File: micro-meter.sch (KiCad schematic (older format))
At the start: 143 parts, among them J1 DC_IN, J10 5V_OUT, J2 SPI, J3 I2C / UART, J4 IN1, J5 IN2, J6 IN3, J7 IN4, J8 SWD, J9 USB_B_Micro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

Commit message: Layout blocks
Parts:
- added J11: LEDS_DATA, Connector_PinHeader_2.54mm:PinHeader_1x03_P2.54mm_Vertical, symbol Connector:Conn_01x03_Male
- added J12: LEDS_EXT, Connector_PinHeader_2.54mm:PinHeader_1x03_P2.54mm_Vertical, symbol Connector:Conn_01x03_Male
- added TP10: TP_4V3, TestPoint:TestPoint_Pad_2.0x2.0mm, symbol Connector:TestPoint
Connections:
- net CE is gone; now on net CE+I2S2_MCK: J2.3 (Pin_3)
- net +5V: now also J11.1 (Pin_1), J12.1 (Pin_1)
- net GND: now also J11.3 (Pin_3), J12.3 (Pin_3)
- net I2S5_SD: now also J11.2 (Pin_2)
- net at D30.1 (K), D4.1 (K), D5.1 (K)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: now also TP10.1
- net LEDS_EXT: now reaches D29.2 (DOUT)
- net LEDS_EXT: now also J12.2 (Pin_2)
- no-connect marks 19 -> 18
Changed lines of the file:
@@
 U 1 1 5FA0621D
 P 4600 7200
-F 0 "C16" H 4800 7250 50  0000 R CNN
-F 1 "10u" H 4850 7150 50  0000 R CNN
+F 0 "C16" H 4850 7200 50  0000 R CNN
+F 1 "10u" H 4850 7100 50  0000 R CNN
 F 2 "Capacitor_SMD:C_0603_1608Metric" H 4600 7200 50  0001 C CNN
 F 3 "~" H 4600 7200 50  0001 C CNN
@@
 U 1 1 5FDE2D61
 P 4300 6950
-F 0 "FB3" V 4500 6900 50  0000 L CNN
+F 0 "FB3" V 4200 6800 50  0000 L CNN
 F 1 "600@100MHz" V 4400 6700 50  0000 L CNN
 F 2 "Inductor_SMD:L_0805_2012Metric" V 4230 6950 50  0001 C CNN
@@
 Wire Wire Line
 	10400 5600 10400 5550
-NoConn ~ 10700 5950
 Wire Wire Line
 	4000 6950 4200 6950
@@
 U 1 1 60044435
 P 4000 7150
-F 0 "R14" H 3900 7100 50  0000 R CNN
-F 1 "3k9" H 3900 7200 50  0000 R CNN
+F 0 "R14" H 3900 7150 50  0000 R CNN
+F 1 "3k9" H 3900 7250 50  0000 R CNN
 F 2 "Resistor_SMD:R_0603_1608Metric" V 3930 7150 50  0001 C CNN
 F 3 "~" H 4000 7150 50  0001 C CNN
@@
 Wire Notes Line
 	8800 1900 11200 1900
-Wire Notes Line
-	4750 4000 4750 500
 Wire Notes Line
 	2900 4000 2900 6550
@@
 	0    1    1    0
 $EndComp
-Text GLabel 1200 5000 0    50   Input ~ 0
-CE
 Text GLabel 1200 5100 0    50   Input ~ 0
 SPI2_SCK
@@
 Text Notes 550  6350 0    50   ~ 0
 Input voltage range: 5-24V DC
+$Comp
+L Connector:TestPoint TP10
+U 1 1 5FB52136
+P 4000 6700
+F 0 "TP10" V 4050 6950 50  0000 C CNN
+F 1 "TP_4V3" V 3950 7000 50  0000 C CNN
+F 2 "TestPoint:TestPoint_Pad_2.0x2.0mm" H 4000 6700 50  0001 C CNN
+F 3 "~" H 4000 6700 50  0001 C CNN
+	1    4000 6700
+	0    1    -1   0
+$EndComp
+Connection ~ 4000 6700
+$Comp
+L Connector:Conn_01x03_Male J11
+U 1 1 5FB8F99C
+P 4600 3150
+F 0 "J11" H 4650 3400 50  0000 C CNN
+F 1 "LEDS_DATA" V 4550 3150 50  0000 C CNN
+F 2 "Connector_PinHeader_2.54mm:PinHeader_1x03_P2.54mm_Vertical" H 4600 3150 50  0001 C CNN
+F 3 "~" H 4600 3150 50  0001 C CNN
+	1    4600 3150
+	-1   0    0    -1
+$EndComp
+Text GLabel 4400 3700 0    50   Input ~ 0
+LEDS_EXT
+$Comp
+L power:+5V #PWR0131
+U 1 1 5FB91854
+P 4400 3050
+F 0 "#PWR0131" H 4400 2900 50  0001 C CNN
+F 1 "+5V" H 4550 3100 50  0000 C CNN
+F 2 "" H 4400 3050 50  0001 C CNN
+F 3 "" H 4400 3050 50  0001 C CNN
+	1    4400 3050
+	-1   0    0    -1
+$EndComp
+$Comp
+L power:GND #PWR0132
+U 1 1 5FB92B2A
+P 4400 3250
+F 0 "#PWR0132" H 4400 3000 50  0001 C CNN
+F 1 "GND" H 4550 3200 50  0000 C CNN
+F 2 "" H 4400 3250 50  0001 C CNN
+F 3 "" H 4400 3250 50  0001 C CNN
+	1    4400 3250
+	-1   0    0    -1
+$EndComp
+Text GLabel 1200 5000 0    50   Input ~ 0
+CE+I2S2_MCK
+$Comp
+L Connector:Conn_01x03_Male J12
+U 1 1 5FD53931
+P 4600 3700
+F 0 "J12" H 4650 3950 50  0000 C CNN
+F 1 "LEDS_EXT" V 4550 3700 50  0000 C CNN
+F 2 "Connector_PinHeader_2.54mm:PinHeader_1x03_P2.54mm_Vertical" H 4600 3700 50  0001 C CNN
+F 3 "~" H 4600 3700 50  0001 C CNN
+	1    4600 3700
+	-1   0    0    -1
+$EndComp
+Text GLabel 4400 3150 0    50   Input ~ 0
+I2S5_SD
+$Comp
+L power:+5V #PWR0133
+U 1 1 5FD5393C
+P 4400 3600
+F 0 "#PWR0133" H 4400 3450 50  0001 C CNN
+F 1 "+5V" H 4550 3650 50  0000 C CNN
+F 2 "" H 4400 3600 50  0001 C CNN
+F 3 "" H 4400 3600 50  0001 C CNN
+	1    4400 3600
+	-1   0    0    -1
+$EndComp
+$Comp
+L power:GND #PWR0134
+U 1 1 5FD53946
+P 4400 3800
+F 0 "#PWR0134" H 4400 3550 50  0001 C CNN
+F 1 "GND" H 4550 3750 50  0000 C CNN
+F 2 "" H 4400 3800 50  0001 C CNN
+F 3 "" H 4400 3800 50  0001 C CNN
+	1    4400 3800
+	-1   0    0    -1
+$EndComp
+Wire Notes Line
+	4750 50   4750 4000
+Text GLabel 10900 6000 3    50   Output ~ 0
+LEDS_EXT
+Wire Wire Line
+	10900 6000 10900 5950
+Wire Wire Line
+	10900 5950 10700 5950
 $EndSCHEMATC

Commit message: Rough layout
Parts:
- removed TP3: TP_5V, TestPoint:TestPoint_Pad_2.0x2.0mm, symbol Connector:TestPoint
- removed U5: USBLC6-2SC6, Package_TO_SOT_SMD:SOT-23-6, symbol Power_Protection:USBLC6-2SC6
- L1: footprint Inductor_SMD:L_Sunlord_MWSA0518_5.4x5.2mm -> Inductor_SMD:L_TDK_NLV25_2.5x2.0mm
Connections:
- net USB_CON_D+ is gone; now on net USB_D+: J9.3 (D+)
- net USB_CON_D- is gone; now on net USB_D-: J9.2 (D-)
- net +5V: now also J11.3 (Pin_3), J12.3 (Pin_3); no longer J11.1 (Pin_1), J12.1 (Pin_1)
- net GND: now also J11.2 (Pin_2), J12.2 (Pin_2); no longer J11.3 (Pin_3), J12.3 (Pin_3)
- net I2S5_SD: now also J11.1 (Pin_1); no longer J11.2 (Pin_2)
- net LEDS_EXT: now also J12.1 (Pin_1); no longer J12.2 (Pin_2)
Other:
- note added: "USB connector"
- note removed: "USB connector + ESD protection"
- moved on the sheet: J9
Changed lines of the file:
@@
 L Connector:USB_B_Micro J9
 U 1 1 5FE0B06F
-P 10800 2500
-F 0 "J9" H 10857 2967 50  0000 C CNN
-F 1 "USB_B_Micro" H 10857 2876 50  0000 C CNN
-F 2 "Connector_USB:USB_Micro-B_Wuerth_629105150521" H 10950 2450 50  0001 C CNN
-F 3 "~" H 10950 2450 50  0001 C CNN
-	1    10800 2500
+P 10100 2900
+F 0 "J9" H 10157 3367 50  0000 C CNN
+F 1 "USB_B_Micro" H 10157 3276 50  0000 C CNN
+F 2 "Connector_USB:USB_Micro-B_Wuerth_629105150521" H 10250 2850 50  0001 C CNN
+F 3 "~" H 10250 2850 50  0001 C CNN
+	1    10100 2900
 	-1   0    0    -1
 $EndComp
@@
 L power:GND #PWR0127
 U 1 1 5FED51E9
-P 10800 2900
-F 0 "#PWR0127" H 10800 2650 50  0001 C CNN
-F 1 "GND" H 10800 2750 50  0000 C CNN
-F 2 "" H 10800 2900 50  0001 C CNN
-F 3 "" H 10800 2900 50  0001 C CNN
-	1    10800 2900
-	-1   0    0    -1
-$EndComp
-NoConn ~ 10900 2900
-NoConn ~ 10500 2700
-Text GLabel 10500 2500 0    50   Output ~ 0
-USB_CON_D+
-Text GLabel 10500 2600 0    50   Output ~ 0
-USB_CON_D-
-$Comp
-L power:GND #PWR0117
-U 1 1 5FEF87AC
-P 9950 3750
-F 0 "#PWR0117" H 9950 3500 50  0001 C CNN
-F 1 "GND" H 9950 3600 50  0000 C CNN
-F 2 "" H 9950 3750 50  0001 C CNN
-F 3 "" H 9950 3750 50  0001 C CNN
-	1    9950 3750
-	1    0    0    -1
-$EndComp
-$Comp
-L power:+5V #PWR0116
-U 1 1 5FEF8E42
-P 9950 2950
-F 0 "#PWR0116" H 9950 2800 50  0001 C CNN
-F 1 "+5V" H 9950 3100 50  0000 C CNN
-F 2 "" H 9950 2950 50  0001 C CNN
-F 3 "" H 9950 2950 50  0001 C CNN
-	1    9950 2950
-	1    0    0    -1
-$EndComp
-Text GLabel 9550 3250 0    50   Input ~ 0
-USB_CON_D+
-Text GLabel 10350 3250 2    50   Input ~ 0
-USB_CON_D-
-Text GLabel 9550 3450 0    50   Output ~ 0
+P 10100 3300
+F 0 "#PWR0127" H 10100 3050 50  0001 C CNN
+F 1 "GND" H 10100 3150 50  0000 C CNN
+F 2 "" H 10100 3300 50  0001 C CNN
+F 3 "" H 10100 3300 50  0001 C CNN
+	1    10100 3300
+	-1   0    0    -1
+$EndComp
+NoConn ~ 10200 3300
+NoConn ~ 9800 3100
+Text GLabel 9800 2900 0    50   Output ~ 0
 USB_D+
-Text GLabel 10350 3450 2    50   Output ~ 0
+Text GLabel 9800 3000 0    50   Output ~ 0
 USB_D-
 $Comp
@@
 Text GLabel 3500 7350 3    50   Input ~ 0
 VBUS
-Text GLabel 10500 2300 0    50   Output ~ 0
+Text GLabel 9800 2700 0    50   Output ~ 0
 VBUS
 Text GLabel 10900 4850 3    50   Output ~ 0
@@
 Serial wire debug header
 Text Notes 8850 2000 0    50   ~ 0
-USB connector + ESD protection
+USB connector
 Text Notes 550  600  0    50   ~ 0
 MCU
@@
 $EndComp
 $Comp
-L Power_Protection:USBLC6-2SC6 U5
-U 1 1 5FEA7054
-P 9950 3350
-F 0 "U5" H 9700 3700 50  0000 C CNN
-F 1 "USBLC6-2SC6" H 10300 3000 50  0000 C CNN
-F 2 "Package_TO_SOT_SMD:SOT-23-6" H 9950 2850 50  0001 C CNN
-F 3 "http://ww1.microchip.com/downloads/en/DeviceDoc/21733j.pdf" H 10150 3700 50  0001 C CNN
-	1    9950 3350
-	1    0    0    -1
-$EndComp
-$Comp
 L Device:Crystal_GND24_Small Y1
 U 1 1 5FA807EB
@@
 Wire Wire Line
 	2800 6700 2900 6700
-$Comp
-L Connector:TestPoint TP3
-U 1 1 604DFC1D
-P 3200 7500
-F 0 "TP3" H 3350 7550 50  0000 C CNN
-F 1 "TP_5V" H 3200 7700 50  0000 C CNN
-F 2 "TestPoint:TestPoint_Pad_2.0x2.0mm" H 3200 7500 50  0001 C CNN
-F 3 "~" H 3200 7500 50  0001 C CNN
-	1    3200 7500
-	1    0    0    1
-$EndComp
 Wire Wire Line
 	2250 7000 2900 7000
@@
 Text GLabel 850  7500 2    50   Input ~ 0
 5V_OUT
-Text GLabel 3200 7500 1    50   Input ~ 0
-5V_OUT
 Text GLabel 3400 6750 3    50   Output ~ 0
 5V_OUT
@@
 F 0 "L1" V 2885 6700 50  0000 C CNN
 F 1 "10u" V 2794 6700 50  0000 C CNN
-F 2 "Inductor_SMD:L_Sunlord_MWSA0518_5.4x5.2mm" H 2700 6700 50  0001 C CNN
-F 3 "~" H 2700 6700 50  0001 C CNN
+F 2 "Inductor_SMD:L_TDK_NLV25_2.5x2.0mm" H 2700 6700 50  0001 C CNN
+F 3 "C98353" H 2700 6700 50  0001 C CNN
 	1    2700 6700
 	0    -1   -1   0
@@
 	-1   0    0    -1
 $EndComp
-Text GLabel 4400 3700 0    50   Input ~ 0
+Text GLabel 4400 3600 0    50   Input ~ 0
 LEDS_EXT
 $Comp
 L power:+5V #PWR0131
 U 1 1 5FB91854
-P 4400 3050
-F 0 "#PWR0131" H 4400 2900 50  0001 C CNN
-F 1 "+5V" H 4550 3100 50  0000 C CNN
-F 2 "" H 4400 3050 50  0001 C CNN
-F 3 "" H 4400 3050 50  0001 C CNN
-	1    4400 3050
-	-1   0    0    -1
-$EndComp
-$Comp
-L power:GND #PWR0132
-U 1 1 5FB92B2A
 P 4400 3250
-F 0 "#PWR0132" H 4400 3000 50  0001 C CNN
-F 1 "GND" H 4550 3200 50  0000 C CNN
+F 0 "#PWR0131" H 4400 3100 50  0001 C CNN
+F 1 "+5V" V 4400 3450 50  0000 C CNN
 F 2 "" H 4400 3250 50  0001 C CNN
 F 3 "" H 4400 3250 50  0001 C CNN
 	1    4400 3250
-	-1   0    0    -1
+	0    -1   1    0
+$EndComp
+$Comp
+L power:GND #PWR0132
+U 1 1 5FB92B2A
+P 4400 3150
+F 0 "#PWR0132" H 4400 2900 50  0001 C CNN
+F 1 "GND" V 4400 2950 50  0000 C CNN
+F 2 "" H 4400 3150 50  0001 C CNN
+F 3 "" H 4400 3150 50  0001 C CNN
+	1    4400 3150
+	0    1    -1   0
 $EndComp
 Text GLabel 1200 5000 0    50   Input ~ 0
@@
 	-1   0    0    -1
 $EndComp
-Text GLabel 4400 3150 0    50   Input ~ 0
+Text GLabel 4400 3050 0    50   Input ~ 0
 I2S5_SD
-$Comp
-L power:+5V #PWR0133
-U 1 1 5FD5393C
-P 4400 3600
-F 0 "#PWR0133" H 4400 3450 50  0001 C CNN
-F 1 "+5V" H 4550 3650 50  0000 C CNN
-F 2 "" H 4400 3600 50  0001 C CNN
-F 3 "" H 4400 3600 50  0001 C CNN
-	1    4400 3600
-	-1   0    0    -1
-$EndComp
-$Comp
-L power:GND #PWR0134
-U 1 1 5FD53946
-P 4400 3800
-F 0 "#PWR0134" H 4400 3550 50  0001 C CNN
-F 1 "GND" H 4550 3750 50  0000 C CNN
-F 2 "" H 4400 3800 50  0001 C CNN
-F 3 "" H 4400 3800 50  0001 C CNN
-	1    4400 3800
-	-1   0    0    -1
-$EndComp
 Wire Notes Line
 	4750 50   4750 4000
@@
 Wire Wire Line
 	10900 5950 10700 5950
+$Comp
+L power:+5V #PWR0116
+U 1 1 5FD3783E
+P 4400 3800
+F 0 "#PWR0116" H 4400 3650 50  0001 C CNN
+F 1 "+5V" V 4400 4000 50  0000 C CNN
+F 2 "" H 4400 3800 50  0001 C CNN
+F 3 "" H 4400 3800 50  0001 C CNN
+	1    4400 3800
+	0    -1   1    0
+$EndComp
+$Comp
+L power:GND #PWR?
+U 1 1 5FD4B157
+P 4400 3700
+F 0 "#PWR?" H 4400 3450 50  0001 C CNN
+F 1 "GND" V 4400 3500 50  0000 C CNN
+F 2 "" H 4400 3700 50  0001 C CNN
+F 3 "" H 4400 3700 50  0001 C CNN
+	1    4400 3700
+	0    1    -1   0
+$EndComp
 $EndSCHEMATC

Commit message: Cleanup layout
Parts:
- removed C10, C11, C14, C15, C17, C18, C24, C25, C30, C31, C32, C33, C35, C36, C38, C39, C40, C41, C42, C43, C44, C45, C47, C48: 0.1u, Capacitor_SMD:C_0402_1005Metric, symbol Device:C_Small
- removed D10, D11, D12, D14, D15, D16, D17, D18, D19, D2, D20, D21, D22, D23, D24, D25, D26, D27, D28, D29, D3, D7, D8, D9: WS2812C, LED_SMD:LED_WS2812B_PLCC4_5.0x5.0mm_P3.2mm, symbol LED:WS2812B
- removed J12: LEDS_EXT, Connector_PinHeader_2.54mm:PinHeader_1x03_P2.54mm_Vertical, symbol Connector:Conn_01x03_Male
- removed TP1: TP_DIN, TestPoint:TestPoint_Pad_2.0x2.0mm, symbol Connector:TestPoint
- removed TP2: TP_GND, TestPoint:TestPoint_Loop_D2.50mm_Drill1.0mm, symbol Connector:TestPoint
- L1: footprint Inductor_SMD:L_TDK_NLV25_2.5x2.0mm -> Inductor_SMD:L_Sunlord_MWSA0518_5.4x5.2mm
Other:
- note removed: "Smart-LEDs"

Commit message: Add routing
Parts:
- removed J3: I2C / UART, Connector_PinSocket_2.54mm:PinSocket_2x04_P2.54mm_Vertical, symbol Connector_Generic:Conn_02x04_Odd_Even
- added J12: I2C, Connector_PinSocket_2.54mm:PinSocket_1x03_P2.54mm_Vertical, symbol Connector:Conn_01x03_Male
- added J3: UART, Connector_PinSocket_2.54mm:PinSocket_1x03_P2.54mm_Vertical, symbol Connector:Conn_01x03_Male
- J4: value IN1 -> IN3
- J5: value IN2 -> IN4
- J6: value IN3 -> IN1
- J7: value IN4 -> IN2
- TP6: value TP_AIN0 -> TP_AIN2
- TP7: value TP_AIN1 -> TP_AIN3
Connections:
- net AIN0: now also J6.1 (Pin_1); no longer C26.2, R24.1, TP6.1, U4.1
- net AIN1: now also J7.1 (Pin_1); no longer C28.2, R27.1, TP7.1, U4.7
- net AIN2: now also C26.2, R24.1, TP6.1, U4.1; no longer J6.1 (Pin_1)
- net AIN3: now also C28.2, R27.1, TP7.1, U4.7; no longer J7.1 (Pin_1)
- net GND: now also J12.2 (Pin_2), J3.2 (Pin_2)
- net I2C1_SCL: now also J12.1 (Pin_1)
- net I2C1_SDA: now also J12.3 (Pin_3)
- net USART1_RX: now also J3.1 (Pin_1)
- net USART1_TX: now also J3.3 (Pin_3)
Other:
- moved on the sheet: J11

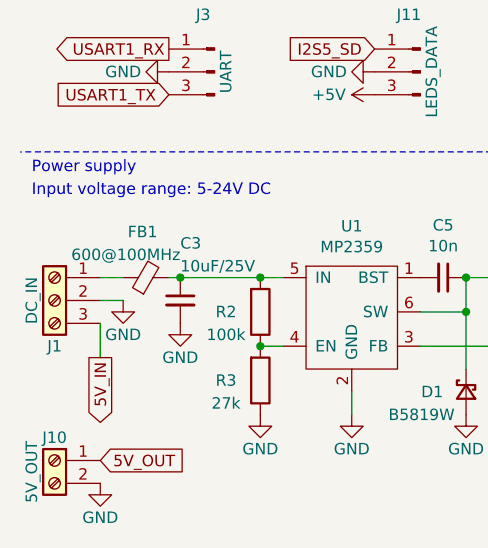
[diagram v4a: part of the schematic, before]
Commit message: Cleanup routing
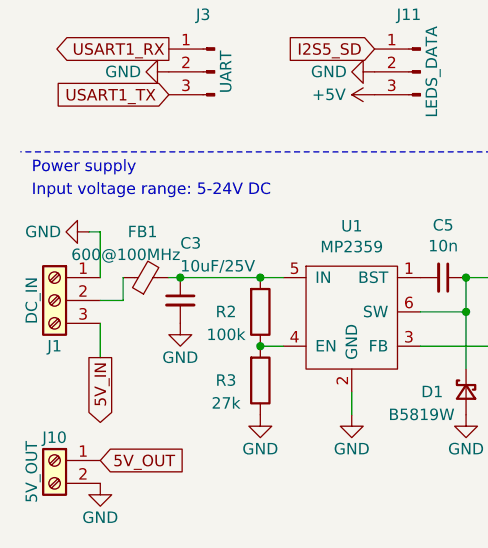
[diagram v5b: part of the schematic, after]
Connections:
- net GND: now also J1.1 (Pin_1); no longer J1.2 (Pin_2)
- net at FB1.1: now also J1.2 (Pin_2); no longer J1.1 (Pin_1)
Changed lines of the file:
@@
 L power:GND #PWR02
 U 1 1 5FECE14C
-P 950 6800
-F 0 "#PWR02" H 950 6550 50  0001 C CNN
-F 1 "GND" H 950 6650 50  0000 C CNN
-F 2 "" H 950 6800 50  0001 C CNN
-F 3 "" H 950 6800 50  0001 C CNN
-	1    950  6800
-	1    0    0    -1
+P 800 6500
+F 0 "#PWR02" H 800 6250 50  0001 C CNN
+F 1 "GND" V 800 6300 50  0000 C CNN
+F 2 "" H 800 6500 50  0001 C CNN
+F 3 "" H 800 6500 50  0001 C CNN
+	1    800  6500
+	0    1    1    0
 $EndComp
 $Comp
@@
 Wire Wire Line
 	3750 6950 4000 6950
-Wire Wire Line
-	850  6700 950  6700
 $Comp
 L Connector:Screw_Terminal_01x02 J10
@@
 	0    -1   1    0
 $EndComp
+Wire Wire Line
+	950  6800 950  6700
+Wire Wire Line
+	850  6700 850  6500
+Wire Wire Line
+	850  6500 800  6500
 $EndSCHEMATC
